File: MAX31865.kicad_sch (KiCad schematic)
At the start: 25 parts, among them U1 MAX31865, U3 MIC5225-3.3, X1 3.5mm, X2 3.5mm

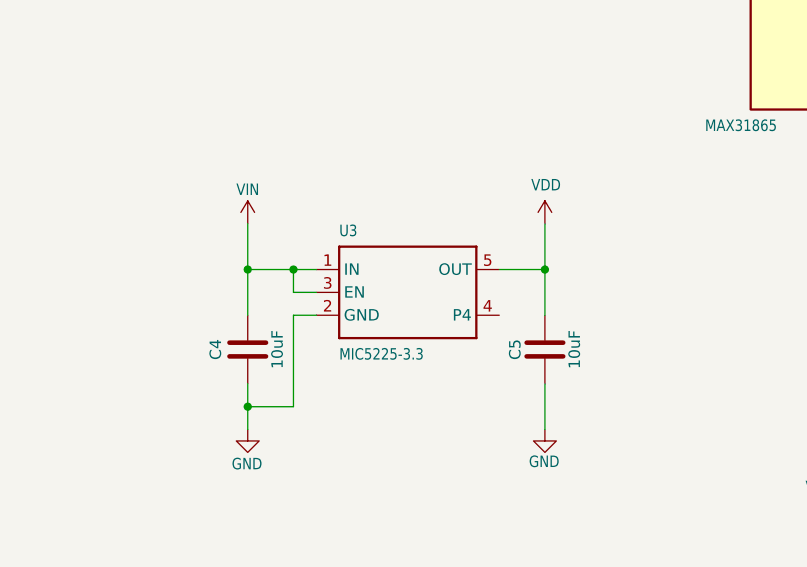
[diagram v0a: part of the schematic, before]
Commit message: changed to own library
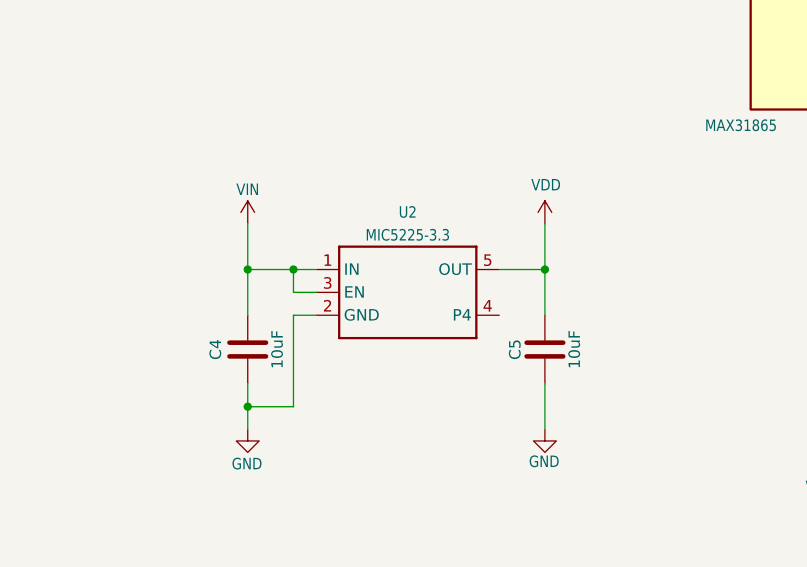
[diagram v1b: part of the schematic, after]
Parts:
- removed U3: MIC5225-3.3, MAX31865:SOT23-5, symbol MAX31865-eagle-import:VREG_SOT23-5
- added U2: MIC5225-3.3, MAX31865:SOT23-5, symbol VREG_SOT23-5:VREG_SOT23-5
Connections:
- net GND: now also U2.2 (GND)
- net VDD: now also U2.5 (OUT)
- net VIN: now also U2.1 (IN), U2.3 (EN)
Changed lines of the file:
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@@
+	)
+	(symbol
+		(lib_id "VREG_SOT23-5:VREG_SOT23-5")
+		(at 78.74 132.08 0)
+		(unit 1)
+		(exclude_from_sim no)
+		(in_bom yes)
+		(on_board yes)
+		(dnp no)
+		(fields_autoplaced yes)
+		(property "Reference" "U2"
+			(at 78.74 123.19 0)
+			(effects
+				(font
+					(size 1.27 1.0795)
+				)
+			)
+		)
+		(property "Value" "MIC5225-3.3"
+			(at 78.74 125.73 0)
+			(effects
+				(font
+					(size 1.27 1.0795)
+				)
+			)
+		)
+		(property "Footprint" "MAX31865:SOT23-5"
+			(at 78.74 132.08 0)
+			(effects
+				(font
+					(size 1.27 1.27)
+				)
+				(hide yes)
+			)
+		)
+		(property "Datasheet" ""
+			(at 78.74 132.08 0)
+			(effects
+				(font
+					(size 1.27 1.27)
+				)
+				(hide yes)
+			)
+		)
+		(property "Description" "SOT23-5 Fixed Voltage Regulators\n\nPart Current Out V Out V In V Dropout θJA (°C/W) TJ (°C) Digikey Part No.     ADP121   150mA   3.3V   3.4-5.5V   0.09V @ 150mA   --   --   ADP121-AUJZ33R7CT-ND     ADP121   150mA   3.0V   3.1-5.5V   0.09V @ 150mA   --   --   ADP121-AUJZ30R7CT-ND     ADP122   300mA   3.3V   3.4-5.5V   0.085V @ 300mA   --   --   ADP122AUJZ-3.3-R7CT-ND     ADP1712   300mA   3.3V   3.5-5.5V   0.17V @ 300mA   --   --   ADP1712AUJZ-3.3-R7TR-ND     AP7311 (Low Cost)   150mA   3.3V   3.5-6V   0.15V @ 150mA   --   --   AP7311-33WG-7DICT-ND      LD39015M18R   150mA   1.8V   1.9V-5.5V   0.08V @ 100mA   --   --   497-6977-1-ND      LP2985A-33DBVR   150mA   3.3V   3.3-16V   0.28V @ 150mA   206   150   296-18479-1-ND      MCP1824T-3302E/OT   300mA   3.3V   3.5V-6V   0.2V @ 300mA   --   --   MCP1824T-3302E/OTCT-ND      MIC5205-2.5YM5 TR   150mA   2.5V   2.7-16V   0.165V @ 150mA   --   --   576-1257-2-ND     MIC5205-3.0YM5 TR   150mA   3.0V   3.2V-16V   0.165V @ 150mA   --   --   576-1258-2-ND     MIC5205-3.3YM5 TR   150mA   3.3V   3.5V-16V   0.165V @ 150mA   --   --   576-1259-2-ND     TPS780330220   150mA   3.3V+2.2V   3.6-5.5V   250mV Max   --   --   296-23332-1-ND     TDA3663/N1,135   100mA   3.3V   3.5-45V   0.18V @ 50mA   --   --   568-5343-1-ND\n\nMax operating temp can be calculated using θJA, TJ (max junction temperature), and power in watts.  Set the \"Maximum Ambient Temperature\" until it reaches TJ (\"Max Junction Temperature\"), which is the absolute limit for safe use of the regulator: http://www.daycounter.com/Calculators/Heat-Sink-Temperature-Calculator.phtml Heat Sink Temperature Calculator\n\nFor example, With 12V source into a 3.3V LP2985 and a 30mA load, we are dissipating (12V-3.3V) * 0.03A = 0.261W.  With a θJA of 206 °C/W, a TJ of 150°C, and 261mW we can safely use the chip without a heat sink up to 75°C (=147.1°C Junction Temperature)."
+			(at 78.74 132.08 0)
+			(effects
+				(font
+					(size 1.27 1.27)
+				)
+				(hide yes)
+			)
+		)
+		(pin "3"
+		)
+		(pin "2"
+		)
+		(pin "4"
+		)
+		(pin "1"
+		)
+		(pin "5"
+		)
+		(instances
+			(project "MAX31865"
+				(path "/7d3dfe06-ad22-4135-8721-3b06d69e4560"
+					(reference "U2")
+					(unit 1)
+				)
+			)
+		)
 	)
 	(symbol
@@
 					(unit 1)
 				)
-			)
-		)
-	)
-	(symbol
-		(lib_id "MAX31865-eagle-import:VREG_SOT23-5")
-		(at 78.74 132.08 0)
-		(unit 1)
-		(exclude_from_sim no)
-		(in_bom yes)
-		(on_board yes)
-		(dnp no)
-		(property "Reference" "U3"
-			(at 71.12 125.984 0)
-			(effects
-				(font
-					(size 1.27 1.0795)
-				)
-				(justify left bottom)
-			)
-		)
-		(property "Value" "MIC5225-3.3"
-			(at 71.12 139.7 0)
-			(effects
-				(font
-					(size 1.27 1.0795)
-				)
-				(justify left bottom)
-			)
-		)
-		(property "Footprint" "MAX31865:SOT23-5"
-			(at 78.74 132.08 0)
-			(effects
-				(font
-					(size 1.27 1.27)
-				)
-				(hide yes)
-			)
-		)
-		(property "Datasheet" ""
-			(at 78.74 132.08 0)
-			(effects
-				(font
-					(size 1.27 1.27)
-				)
-				(hide yes)
-			)
-		)
-		(property "Description" ""
-			(at 78.74 132.08 0)
-			(effects
-				(font
-					(size 1.27 1.27)
-				)
-				(hide yes)
-			)
-		)
-		(pin "1"
-		)
-		(pin "2"
-		)
-		(pin "3"
-		)
-		(pin "4"
-		)
-		(pin "5"
-		)
-		(instances
-			(project "MAX31865"
-				(path "/7d3dfe06-ad22-4135-8721-3b06d69e4560"
-					(reference "U3")
-					(unit 1)
-				)

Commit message: changed all capacitor foorprints in schematic
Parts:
- C1, C2, C3, C4, C5: footprint MAX31865:0805-NO -> Capacitor_SMD:C_0805_2012Metric
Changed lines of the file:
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@@
 			)
 		)
-		(property "Footprint" "MAX31865:0805-NO"
+		(property "Footprint" "Capacitor_SMD:C_0805_2012Metric"
 			(at 94.9452 142.24 0)
 			(effects
@@
 			)
 		)
-		(property "Footprint" "MAX31865:0805-NO"
+		(property "Footprint" "Capacitor_SMD:C_0805_2012Metric"
 			(at 140.6652 60.96 0)
 			(effects
@@
 			)
 		)
-		(property "Footprint" "MAX31865:0805-NO"
+		(property "Footprint" "Capacitor_SMD:C_0805_2012Metric"
 			(at 163.5252 116.84 0)
 			(effects
@@
 			)
 		)
-		(property "Footprint" "MAX31865:0805-NO"
+		(property "Footprint" "Capacitor_SMD:C_0805_2012Metric"
 			(at 120.3452 55.88 0)
 			(effects
@@
 			)
 		)
-		(property "Footprint" "MAX31865:0805-NO"
+		(property "Footprint" "Capacitor_SMD:C_0805_2012Metric"
 			(at 61.9252 142.24 0)
 			(effects

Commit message: changed all resistor footprints in schematic
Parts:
- R1, R6, R7, R8: footprint MAX31865:0805-NO -> Resistor_SMD:R_0805_2012Metric
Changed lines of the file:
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@@
 			)
 		)
-		(property "Footprint" "MAX31865:0805-NO"
+		(property "Footprint" "Resistor_SMD:R_0805_2012Metric"
 			(at 100.838 77.47 90)
 			(effects
@@
 			)
 		)
-		(property "Footprint" "MAX31865:0805-NO"
+		(property "Footprint" "Resistor_SMD:R_0805_2012Metric"
 			(at 169.418 80.01 90)
 			(effects
@@
 			)
 		)
-		(property "Footprint" "MAX31865:0805-NO"
+		(property "Footprint" "Resistor_SMD:R_0805_2012Metric"
 			(at 95.758 69.85 90)
 			(effects
@@
 			)
 		)
-		(property "Footprint" "MAX31865:0805-NO"
+		(property "Footprint" "Resistor_SMD:R_0805_2012Metric"
 			(at 93.218 77.47 90)
 			(effects

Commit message: changed all diode footprints in schematic
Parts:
- D1, D2, D3: footprint MAX31865:SOD-323 -> Diode_SMD:D_SOD-323
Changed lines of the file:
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@@
 			)
 		)
-		(property "Footprint" "MAX31865:SOD-323"
+		(property "Footprint" "Diode_SMD:D_SOD-323"
 			(at 73.66 83.82 0)
 			(effects
@@
 			)
 		)
-		(property "Footprint" "MAX31865:SOD-323"
+		(property "Footprint" "Diode_SMD:D_SOD-323"
 			(at 76.2 78.74 0)
 			(effects
@@
 			)
 		)
-		(property "Footprint" "MAX31865:SOD-323"
+		(property "Footprint" "Diode_SMD:D_SOD-323"
 			(at 76.2 73.66 0)
 			(effects

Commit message: changed all connectors footprints in schematic
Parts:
- X1, X2: footprint MAX31865:TERMBLOCK_1X2-3.5MM -> TerminalBlock_4Ucon:TerminalBlock_4Ucon_1x02_P3.50mm_Horizontal
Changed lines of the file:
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@@
 			)
 		)
-		(property "Footprint" "MAX31865:TERMBLOCK_1X2-3.5MM"
+		(property "Footprint" "TerminalBlock_4Ucon:TerminalBlock_4Ucon_1x02_P3.50mm_Horizontal"
 			(at 190.5 119.38 0)
 			(effects
@@
 			)
 		)
-		(property "Footprint" "MAX31865:TERMBLOCK_1X2-3.5MM"
+		(property "Footprint" "TerminalBlock_4Ucon:TerminalBlock_4Ucon_1x02_P3.50mm_Horizontal"
 			(at 190.5 99.06 0)
 			(effects

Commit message: changed connector pin 1x08 footprints in schematic
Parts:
- JP1: footprint MAX31865:1X08_ROUND_70 -> Connector_PinHeader_1.00mm:PinHeader_1x08_P1.00mm_Vertical
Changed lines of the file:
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@@
 			)
 		)
-		(property "Footprint" "MAX31865:1X08_ROUND_70"
+		(property "Footprint" "Connector_PinHeader_1.00mm:PinHeader_1x08_P1.00mm_Vertical"
 			(at 142.24 172.72 0)
 			(effects

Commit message: changed solder footprint in schematic and pcb layout
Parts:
- SJ3, SJ4: footprint MAX31865:SOLDERJUMPER_ARROW_NOPASTE -> Jumper:SolderJumper-2_P1.3mm_Open_RoundedPad1.0x1.5mm
- U$18, U$19: footprint MAX31865:MOUNTINGHOLE_2.5_PLATED -> MountingHole:MountingHole_2.5mm
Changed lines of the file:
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@@
 			)
 		)
-		(property "Footprint" "MAX31865:SOLDERJUMPER_ARROW_NOPASTE"
+		(property "Footprint" "Jumper:SolderJumper-2_P1.3mm_Open_RoundedPad1.0x1.5mm"
 			(at 177.8 121.92 0)
 			(effects
@@
 			)
 		)
-		(property "Footprint" "MAX31865:SOLDERJUMPER_ARROW_NOPASTE"
+		(property "Footprint" "Jumper:SolderJumper-2_P1.3mm_Open_RoundedPad1.0x1.5mm"
 			(at 177.8 101.6 0)
 			(effects
@@
 			)
 		)
-		(property "Footprint" "MAX31865:MOUNTINGHOLE_2.5_PLATED"
+		(property "Footprint" "MountingHole:MountingHole_2.5mm"
 			(at 73.66 40.64 0)
 			(effects
@@
 			)
 		)
-		(property "Footprint" "MAX31865:MOUNTINGHOLE_2.5_PLATED"
+		(property "Footprint" "MountingHole:MountingHole_2.5mm"
 			(at 38.1 40.64 0)
 			(effects

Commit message: changed sot-23-5 footprint in schematic and pcb layout
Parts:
- FID1, FID2: footprint MAX31865:FIDUCIAL_1MM -> Fiducial:Fiducial_1mm_Mask2mm
- U2: footprint MAX31865:SOT23-5 -> Package_TO_SOT_SMD:SOT-23-5
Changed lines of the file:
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@@
 			)
 		)
-		(property "Footprint" "MAX31865:SOT23-5"
+		(property "Footprint" "Package_TO_SOT_SMD:SOT-23-5"
 			(at 78.74 132.08 0)
 			(effects
@@
 			)
 		)
-		(property "Footprint" "MAX31865:FIDUCIAL_1MM"
+		(property "Footprint" "Fiducial:Fiducial_1mm_Mask2mm"
 			(at 271.78 157.48 0)
 			(effects
@@
 			)
 		)
-		(property "Footprint" "MAX31865:FIDUCIAL_1MM"
+		(property "Footprint" "Fiducial:Fiducial_1mm_Mask2mm"
 			(at 266.7 157.48 0)
 			(effects
